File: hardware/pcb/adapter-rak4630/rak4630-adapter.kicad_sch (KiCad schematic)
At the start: 22 parts, among them J3 USB-C, SW1 RESET, U3 USBLC6-2SC6, U4 RAK4630-8-SM-I, U5 RV-3028-C7

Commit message: Updated RAK4630 board
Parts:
- added C10, C11: 100u 6.3V, rak4630-adapter:CPH3225A, symbol adapter:C
- C3, C6, C9: LCSC Part # (none) -> C49678
- C4: LCSC Part # (none) -> C15850
- C5: LCSC Part # (none) -> C1779
- C7: value CPH3225A 11mF -> 100u 6.3V; LCSC Part # (none) -> C49066
- C8: value DNP -> 100u 6.3V; LCSC Part # (none) -> C49066; now fitted
- D1: LCSC Part # (none) -> C2297
- D2: LCSC Part # (none) -> C2293
- J3: LCSC Part # (none) -> C720628
- R1, R2, R3: LCSC Part # (none) -> C17414
- R4, R5: LCSC Part # (none) -> C27834
- R6, R7: LCSC Part # (none) -> C17513
- SW1: LCSC Part # (none) -> C2837531
- U2: now not fitted
- U3: JLCPCB Rotation Offset (none) -> 270; LCSC Part # (none) -> C7519
- U4: LCSC Part # (none) -> C32315253
- U5: JLCPCB Rotation Offset (none) -> 180; LCSC Part # (none) -> C3304278
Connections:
- net +3V3: now also C10.1, C11.1
- net GND: now also C10.2, C11.2
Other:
- note added: "Bulk reservoir for TX bursts 2x 100uF near 3V3 header entry"

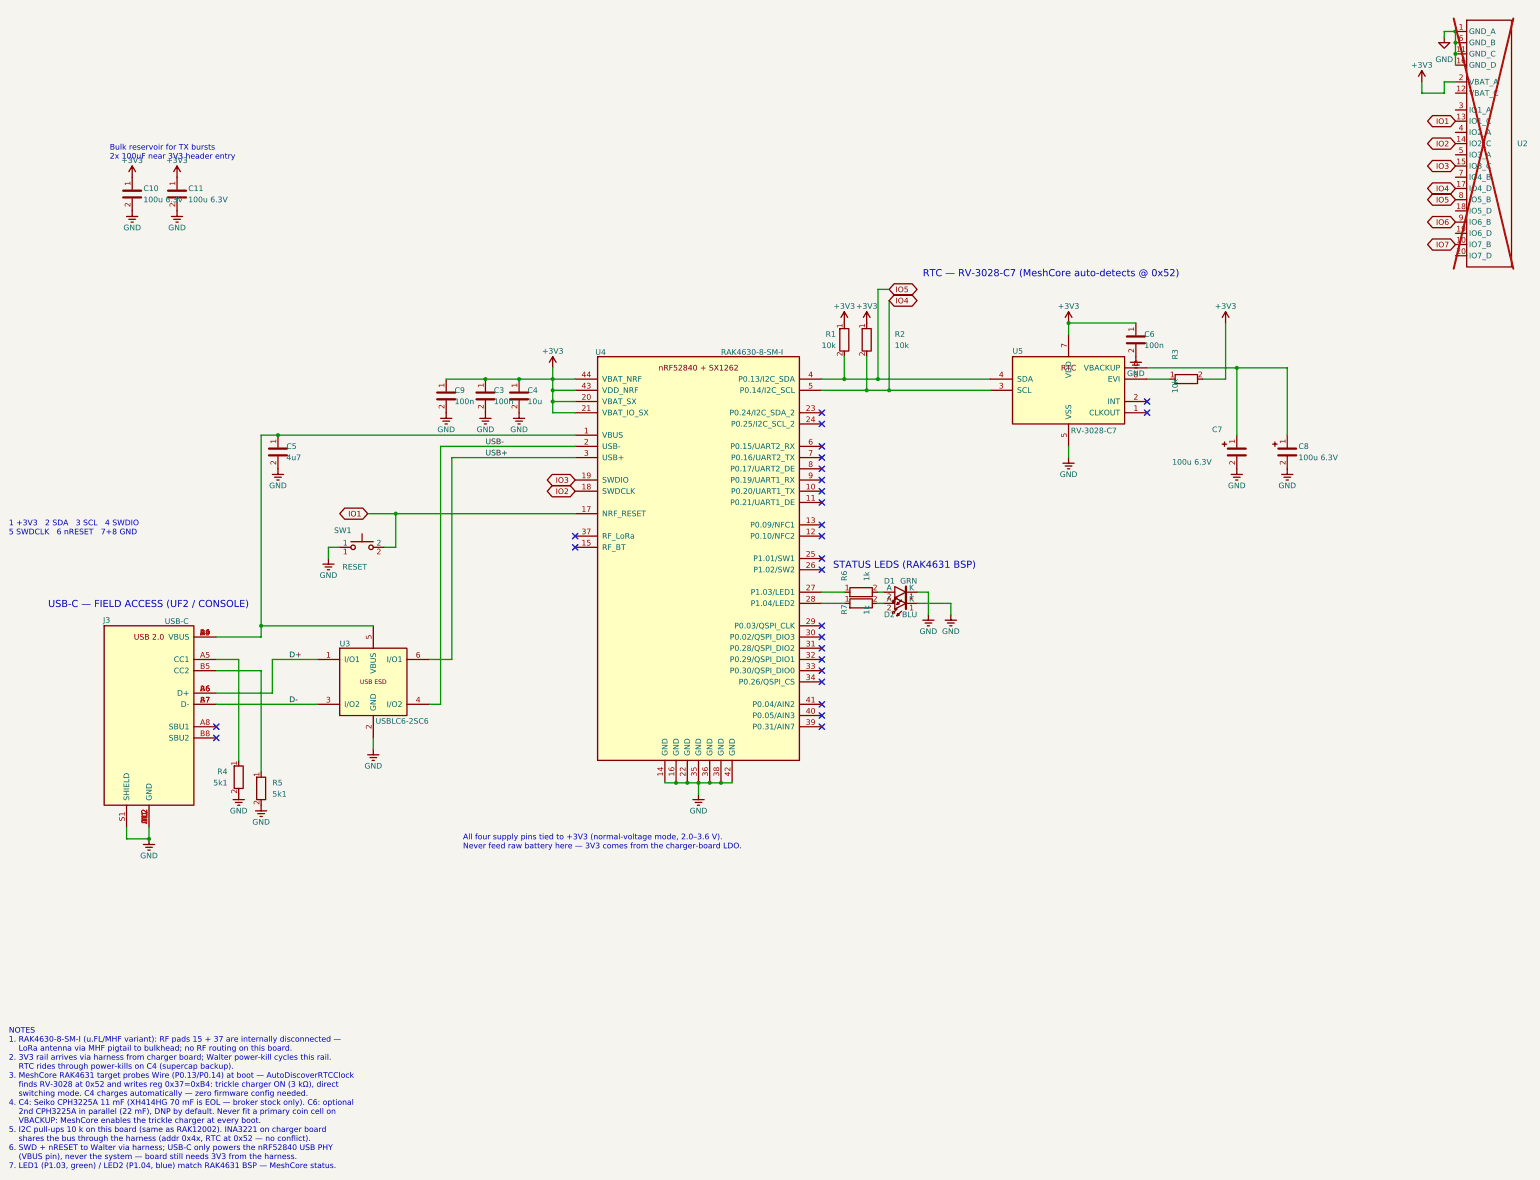
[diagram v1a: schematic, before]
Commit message: Updated RAK4630 adapter
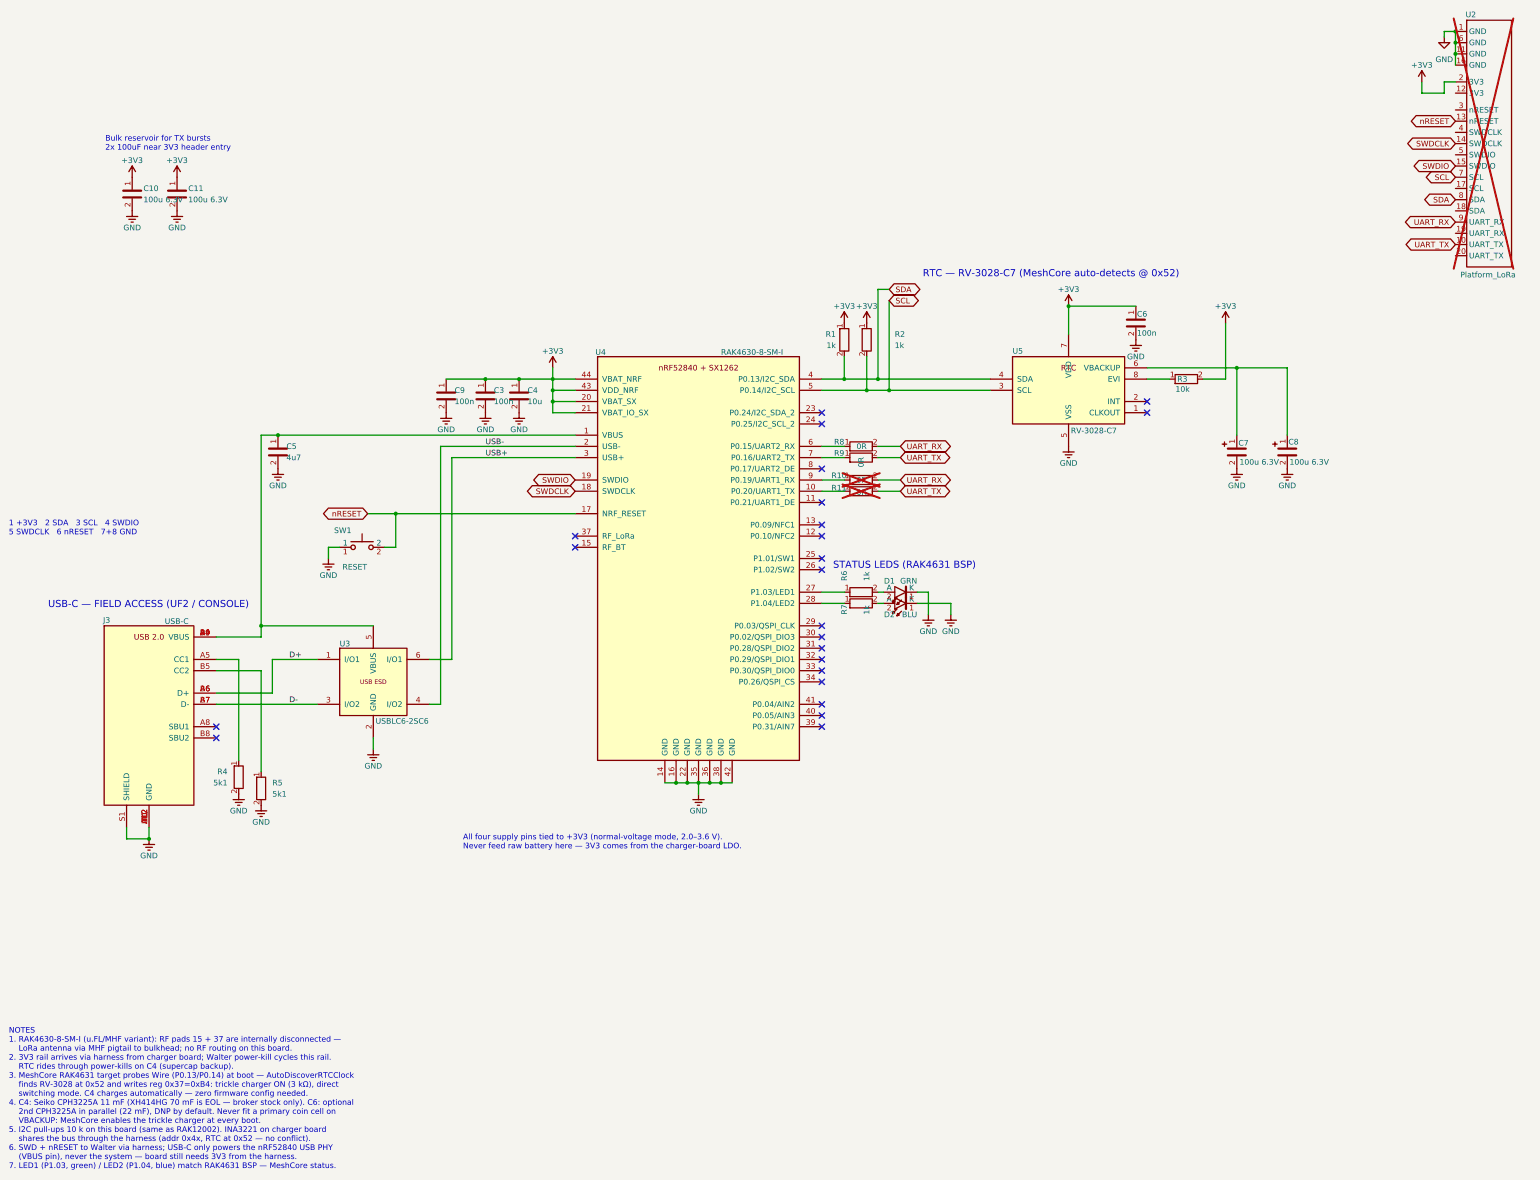
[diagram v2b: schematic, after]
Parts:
- added R10, R11, R8, R9: 0R, Resistor_SMD:R_0805_2012Metric_Pad1.20x1.40mm_HandSolder, symbol adapter:R
- R1, R2: value 10k -> 1k; LCSC Part # C17414 -> C17513
- U2: value (none) -> Platform_LoRa; symbol TwinOak-standard-repeater-layout:Platform_interface -> TwinOak-standard-repeater-layout:Platform_LoRa
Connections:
- net SCL: now reaches U2.7 (SCL)
- net SCL: now also R2.2, U4.5 (P0.14/I2C_SCL), U5.3 (SCL)
- net at U4.10 (P0.20/UART1_TX): now also R11.1
- net at U4.6 (P0.15/UART2_RX): now also R8.1
- net at U4.7 (P0.16/UART2_TX): now also R9.1
- net at U4.9 (P0.19/UART1_RX): now also R10.1
- net IO1 renamed nRESET
- net IO2 renamed SWDCLK
- net IO3 renamed SWDIO
- removed net IO4: R2.2, U2.17 (IO4_D), U4.5 (P0.14/I2C_SCL), U5.3 (SCL)
- net IO5 renamed SDA
- net IO6 renamed UART_RX
- net UART_RX: now also R10.2, R8.2
- net IO7 renamed UART_TX
- net UART_TX: now also R11.2, R9.2
- no-connect marks 27 -> 23
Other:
- moved on the sheet: C6

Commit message: Cleanup
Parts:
- removed R10, R11, R8, R9: 0R, Resistor_SMD:R_0805_2012Metric_Pad1.20x1.40mm_HandSolder, symbol adapter:R
- added J4, J5: SER_SEL, Connector_PinHeader_2.54mm:PinHeader_1x03_P2.54mm_Vertical, symbol Connector:Conn_01x03_Pin
- C10, C11, C7, C8: footprint rak4630-adapter:CPH3225A -> TwinOak:CPH3225A
- J3: footprint rak4630-adapter:USB_C_Receptacle_XUNPU_TYPEC-303-ACP16_Vertical -> TwinOak:USB_C_Receptacle_XUNPU_TYPEC-303-ACP16_Vertical
- SW1: footprint rak4630-adapter:SW_Push_Kinghelm_KH-6X6X5H-STM -> TwinOak:SW_Push_Kinghelm_KH-6X6X5H-STM; symbol adapter:SW_Push -> Switch:SW_Push
- U2: footprint TwinOak platform footprints:platform-adapter-footprint -> TwinOak:platform-adapter-footprint; symbol TwinOak-standard-repeater-layout:Platform_LoRa -> TwinOak:Platform_LoRa
- U4: footprint rak4630-adapter:RAK4630 -> TwinOak:RAK4630; symbol adapter:RAK4630 -> TwinOak:RAK4630
- U5: footprint rak4630-adapter:RV-3028-C7 -> TwinOak:RV-3028-C7; symbol adapter:RV-3028-C7 -> TwinOak:RV-3028-C7
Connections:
- net UART_RX: now also J4.2 (Pin_2)
- net UART_TX: now also J5.2 (Pin_2)
- net SER2_RX: now reaches U4.9 (P0.19/UART1_RX)
- net SER2_RX: now also J4.3 (Pin_3)
- net SER1_TX: now reaches U4.7 (P0.16/UART2_TX)
- net SER1_TX: now also J5.1 (Pin_1)
- net SER1_RX: now reaches U4.6 (P0.15/UART2_RX)
- net SER1_RX: now also J4.1 (Pin_1)
- net SER2_TX: now reaches U4.10 (P0.20/UART1_TX)
- net SER2_TX: now also J5.3 (Pin_3)
- no-connect marks 23 -> 31

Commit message: Adjusted track widths on all boards
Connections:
- net SCL: no longer R2.2
- net SDA: no longer R1.2
- net UART_RX: now also U2.19 (UART_RX); no longer U2.9 (UART_RX)
- net UART_TX: now also U2.20 (UART_TX); no longer U2.10 (UART_TX)
- net at U2.17 (SCL): now also R2.2
- net at U2.18 (SDA): now also R1.2
- no-connect marks 31 -> 29

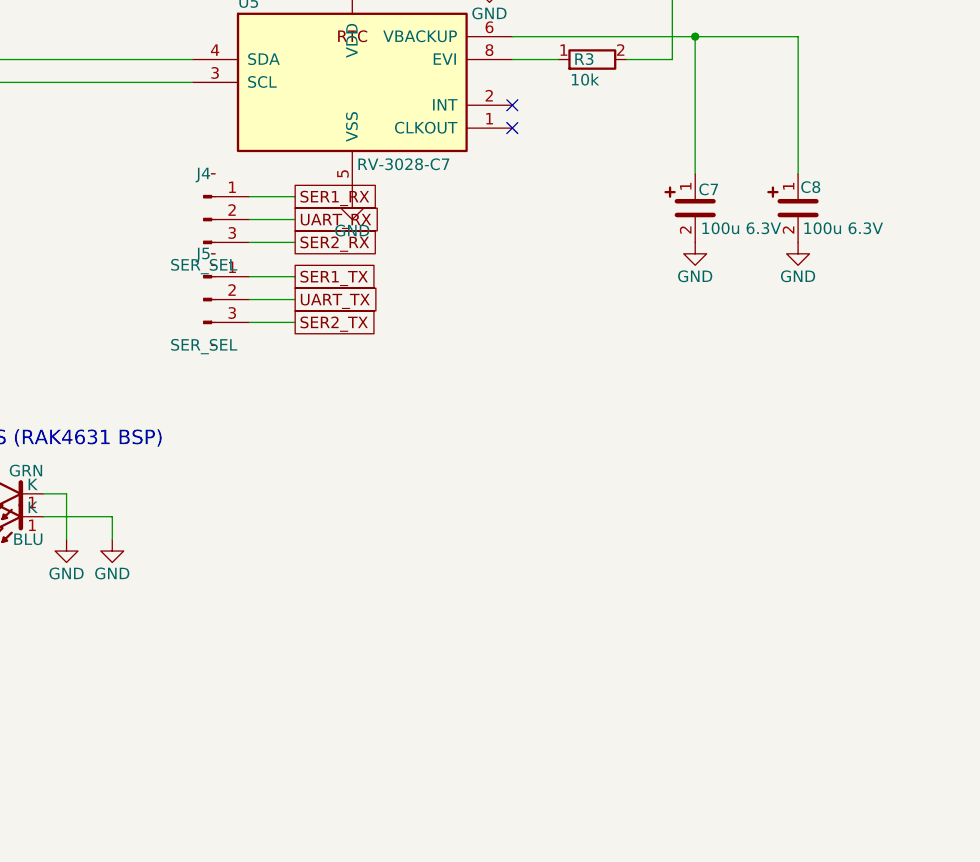
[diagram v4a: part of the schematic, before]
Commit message: Cleanup of schematics and pcb traces on RAK4630 adapter
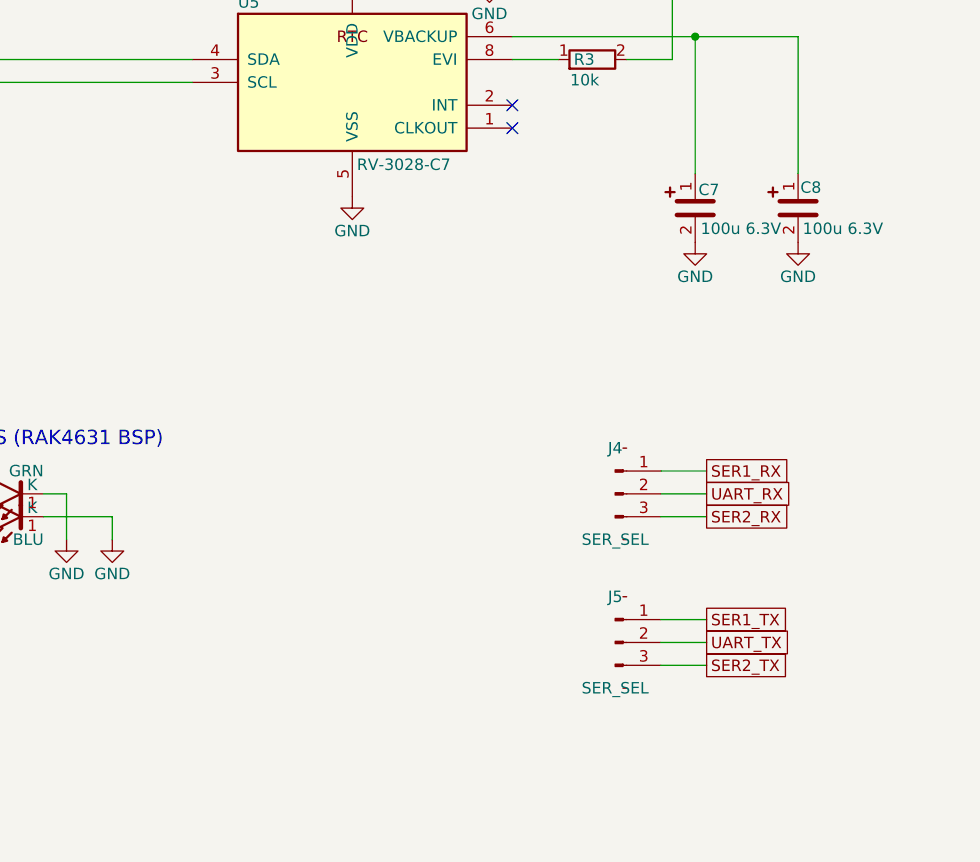
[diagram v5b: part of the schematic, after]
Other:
- moved on the sheet: J4, J5
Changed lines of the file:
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@@
 	(wire
 		(pts
-			(xy 276.86 139.7) (xy 281.94 139.7)
+			(xy 322.58 177.8) (xy 327.66 177.8)
 		)
 		(stroke
@@
 	(wire
 		(pts
-			(xy 276.86 134.62) (xy 281.94 134.62)
+			(xy 322.58 172.72) (xy 327.66 172.72)
 		)
 		(stroke
@@
 	(wire
 		(pts
-			(xy 276.86 130.81) (xy 281.94 130.81)
+			(xy 322.58 161.29) (xy 327.66 161.29)
 		)
 		(stroke
@@
 	(wire
 		(pts
-			(xy 276.86 128.27) (xy 281.94 128.27)
+			(xy 322.58 158.75) (xy 327.66 158.75)
 		)
 		(stroke
@@
 	(wire
 		(pts
-			(xy 276.86 137.16) (xy 281.94 137.16)
+			(xy 322.58 175.26) (xy 327.66 175.26)
 		)
 		(stroke
@@
 	(wire
 		(pts
-			(xy 276.86 125.73) (xy 281.94 125.73)
+			(xy 322.58 156.21) (xy 327.66 156.21)
 		)
 		(stroke
@@
 	(global_label "SER1_TX"
 		(shape passive)
-		(at 281.94 134.62 0)
+		(at 327.66 172.72 0)
 		(effects
 			(font
@@
 		)
 		(property "Intersheetrefs" "${INTERSHEET_REFS}"
-			(at 281.94 134.62 0)
+			(at 327.66 172.72 0)
 			(hide yes)
 			(show_name no)
@@
 	(global_label "SER2_TX"
 		(shape passive)
-		(at 281.94 139.7 0)
+		(at 327.66 177.8 0)
 		(effects
 			(font
@@
 		)
 		(property "Intersheetrefs" "${INTERSHEET_REFS}"
-			(at 281.94 139.7 0)
+			(at 327.66 177.8 0)
 			(hide yes)
 			(show_name no)
@@
 	(global_label "SER1_RX"
 		(shape passive)
-		(at 281.94 125.73 0)
+		(at 327.66 156.21 0)
 		(effects
 			(font
@@
 		)
 		(property "Intersheetrefs" "${INTERSHEET_REFS}"
-			(at 281.94 125.73 0)
+			(at 327.66 156.21 0)
 			(hide yes)
 			(show_name no)
@@
 	(global_label "SER2_RX"
 		(shape passive)
-		(at 281.94 130.81 0)
+		(at 327.66 161.29 0)
 		(effects
 			(font
@@
 		)
 		(property "Intersheetrefs" "${INTERSHEET_REFS}"
-			(at 281.94 130.81 0)
+			(at 327.66 161.29 0)
 			(hide yes)
 			(show_name no)
@@
 	(global_label "UART_RX"
 		(shape passive)
-		(at 281.94 128.27 0)
+		(at 327.66 158.75 0)
 		(effects
 			(font
@@
 		)
 		(property "Intersheetrefs" "${INTERSHEET_REFS}"
-			(at 281.94 128.27 0)
+			(at 327.66 158.75 0)
 			(hide yes)
 			(show_name no)
@@
 	(global_label "UART_TX"
 		(shape passive)
-		(at 281.94 137.16 0)
+		(at 327.66 175.26 0)
 		(effects
 			(font
@@
 		)
 		(property "Intersheetrefs" "${INTERSHEET_REFS}"
-			(at 281.94 137.16 0)
+			(at 327.66 175.26 0)
 			(hide yes)
 			(show_name no)
@@
 	(symbol
 		(lib_id "Connector:Conn_01x03_Pin")
-		(at 271.78 128.27 0)
+		(at 317.5 158.75 0)
 		(unit 1)
 		(body_style 1)
@@
 		(dnp no)
 		(property "Reference" "J4"
-			(at 271.78 123.19 0)
+			(at 317.5 153.67 0)
 			(show_name no)
 			(do_not_autoplace no)
@@
 		)
 		(property "Value" "SER_SEL"
-			(at 271.78 133.35 0)
+			(at 317.5 163.83 0)
 			(show_name no)
 			(do_not_autoplace no)
@@
 		)
 		(property "Footprint" "Connector_PinHeader_2.54mm:PinHeader_1x03_P2.54mm_Vertical"
-			(at 271.78 128.27 0)
+			(at 317.5 158.75 0)
 			(hide yes)
 			(show_name no)
@@
 		)
 		(property "Datasheet" "~"
-			(at 271.78 128.27 0)
+			(at 317.5 158.75 0)
 			(hide yes)
 			(show_name no)
@@
 		)
 		(property "Description" "UART select: jumper 1-2 = Serial1 (P0.15/P0.16, default), jumper 2-3 = Serial2 (P0.19/P0.20)"
-			(at 271.78 128.27 0)
+			(at 317.5 158.75 0)
 			(hide yes)
 			(show_name no)
@@
 	(symbol
 		(lib_id "Connector:Conn_01x03_Pin")
-		(at 271.78 137.16 0)
+		(at 317.5 175.26 0)
 		(unit 1)
 		(body_style 1)
@@
 		(dnp no)
 		(property "Reference" "J5"
-			(at 271.78 132.08 0)
+			(at 317.5 170.18 0)
 			(show_name no)
 			(do_not_autoplace no)
@@
 		)
 		(property "Value" "SER_SEL"
-			(at 271.78 142.24 0)
+			(at 317.5 180.34 0)
 			(show_name no)
 			(do_not_autoplace no)
@@
 		)
 		(property "Footprint" "Connector_PinHeader_2.54mm:PinHeader_1x03_P2.54mm_Vertical"
-			(at 271.78 137.16 0)
+			(at 317.5 175.26 0)
 			(hide yes)
 			(show_name no)
@@
 		)
 		(property "Datasheet" "~"
-			(at 271.78 137.16 0)
+			(at 317.5 175.26 0)
 			(hide yes)
 			(show_name no)
@@
 		)
 		(property "Description" "UART select: jumper 1-2 = Serial1 (P0.15/P0.16, default), jumper 2-3 = Serial2 (P0.19/P0.20)"
-			(at 271.78 137.16 0)
-			(hide yes)
-			(show_name no)
+			(at 317.5 175.26 0)
+			(hide yes)
+			(show_name no)

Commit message: Misc minor updates for production of pcbs
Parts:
- J4, J5, U2: now left out of the parts list
- U3: JLCPCB Rotation Offset 270 -> -90
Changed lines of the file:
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@@
 			)
 		)
-		(property "JLCPCB Rotation Offset" "270"
+		(property "JLCPCB Rotation Offset" "-90"
 			(at 130.81 179.07 0)
 			(hide yes)
@@
 		(body_style 1)
 		(exclude_from_sim no)
-		(in_bom yes)
-		(on_board yes)
-		(in_pos_files yes)
+		(in_bom no)
+		(on_board yes)
+		(in_pos_files no)
 		(dnp no)
 		(property "Reference" "J4"
@@
 		(body_style 1)
 		(exclude_from_sim no)
-		(in_bom yes)
-		(on_board yes)
-		(in_pos_files yes)
+		(in_bom no)
+		(on_board yes)
+		(in_pos_files no)
 		(dnp no)
 		(property "Reference" "J5"
@@
 		(body_style 1)
 		(exclude_from_sim no)
-		(in_bom yes)
-		(on_board yes)
-		(in_pos_files yes)
+		(in_bom no)
+		(on_board yes)
+		(in_pos_files no)
 		(dnp yes)
 		(property "Reference" "U2"
